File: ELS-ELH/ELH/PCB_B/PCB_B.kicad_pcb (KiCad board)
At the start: 2 copper layers, 95 x 95 mm, 47 parts, among them J10 Conn_01x07_Pin, J11 Conn_01x08_Pin, J13 Conn_01x06_Pin, J14 TX2 3V3, J15 RX2 3V3, J16 TX2 5V, J17 RX2 5V, J18 Conn_01x06_Pin, J2 GPS Connector, J3 Conn_01x20_Pin, J4 Conn_01x20_Pin, J7 I2C Bus Connector 3, J8 I2C Bus Connector 2, J9 I2C Bus Connector 1, U1 GY-87

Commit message: PCB B ready, PCB A layout ready
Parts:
- removed J10: Conn_01x07_Pin, Connector_PinHeader_2.54mm:PinHeader_1x07_P2.54mm_Vertical
- J3, J4: footprint Connector_PinHeader_2.54mm:PinHeader_1x20_P2.54mm_Vertical -> Connector_PinSocket_2.54mm:PinSocket_1x20_P2.54mm_Vertical

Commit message: Finish PCB B
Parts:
- added J10: Conn_01x07_Pin, Connector_PinHeader_2.54mm:PinHeader_1x07_P2.54mm_Vertical, F.Cu at (73.1, -0.53)
- turned R1 to 80 degrees
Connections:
- ESP1 pad D2: /D2_ESP_MAIN_3V3 -> /CS_SD_ESP_MAIN_3V3
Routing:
- net /CS_SD_ESP_MAIN_3V3: track 0.00 -> 73.7 mm, vias 0 -> 2
- net +5V_MCU: track 195.8 -> 194.4 mm
- net Net-(ESP2-PadD34): track 63.4 -> 62.7 mm

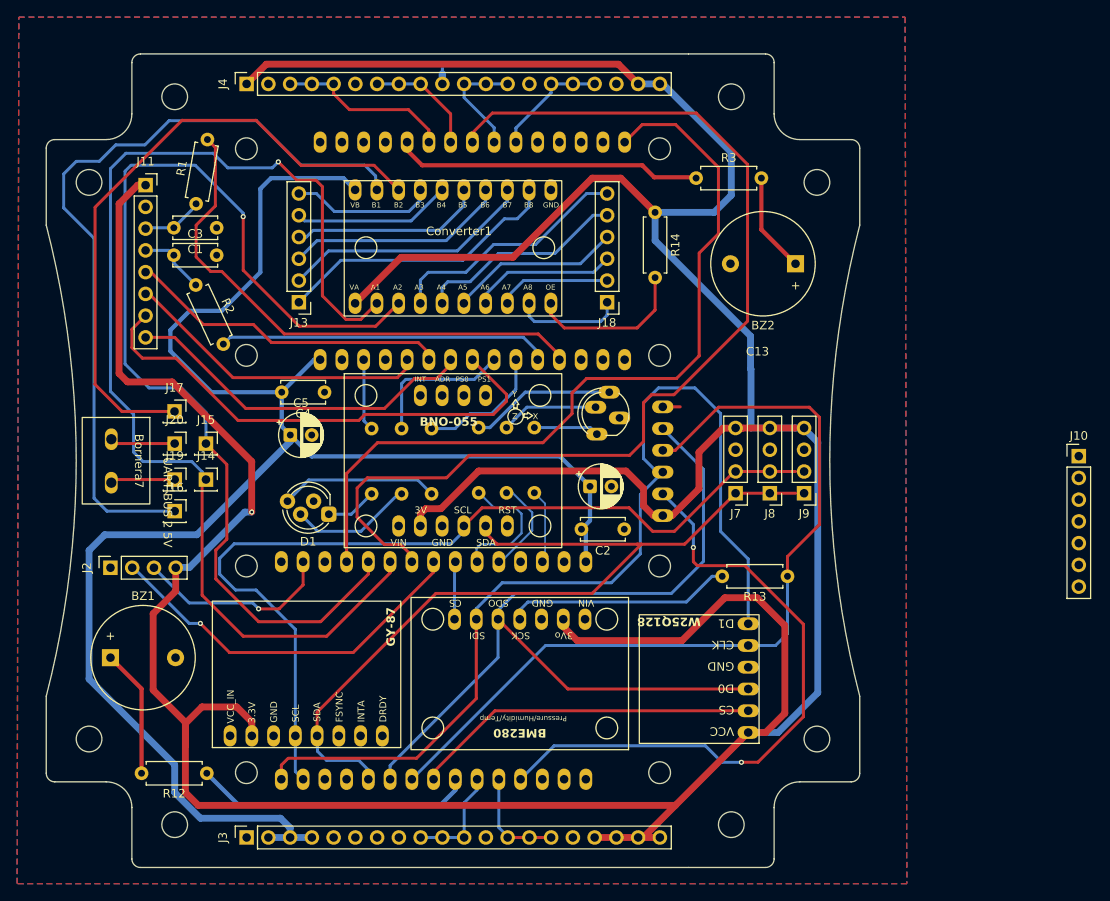
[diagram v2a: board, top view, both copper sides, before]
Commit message: Solve DRC problems with B
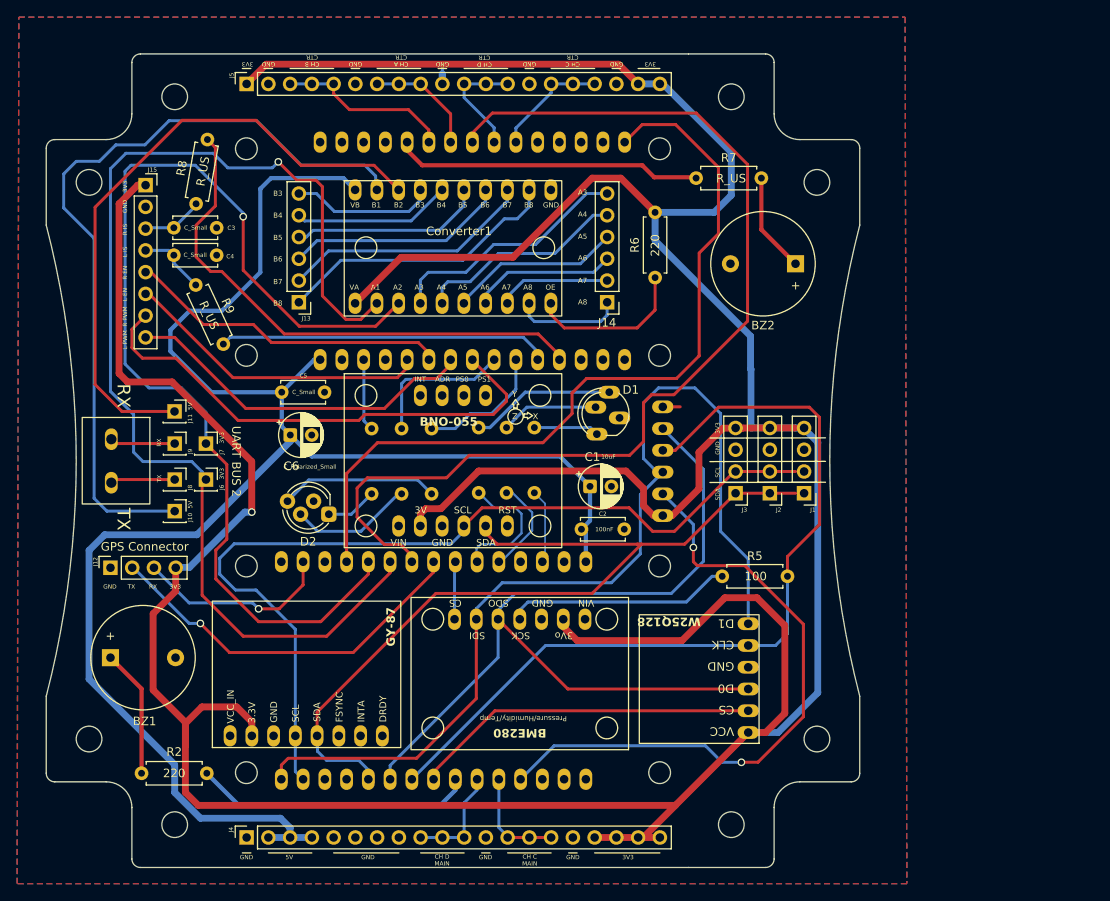
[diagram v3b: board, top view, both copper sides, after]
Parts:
- removed the J10 at (73.1, -0.53)
- Bornera1: renamed from Bornera7; value UART BUS 2 5V -> UART BUS 2
- R10: renamed from R6; value R_US -> 330
- R11: renamed from R8; value R_US -> 330
- R12: renamed from R9; value R_US -> 330
- renumbered BME2 to BME1, C13 to C1, C1 to C3, C3 to C4, C4 to C5, C5 to C6, D10 to D1, D1 to D2, ESP2 to ESP_CTR1, ESP1 to ESP_MAIN1, IMU3 to IMU1, J9 to J1, J16 to J10, J17 to J11, J2 to J12, J18 to J14, J11 to J15, J8 to J2, J7 to J3, J3 to J4, J4 to J5, J14 to J6, J15 to J7, J19 to J8, J20 to J9, R7 to R1, R12 to R2, R5 to R3, R13 to R5, R14 to R6, R3 to R7, R1 to R8, R2 to R9
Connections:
- ESP_MAIN1 pad D12: /D12_ESP_ESP_MAIN_3V3 -> unconnected-(ESP_MAIN1-PadD12)
- ESP_MAIN1 pad D15: /D15_ESP_MAIN_3V3 -> unconnected-(ESP_MAIN1-PadD15)
- ESP_MAIN1 pad EN: /EN_ESP_MAIN_3V3 -> unconnected-(ESP_MAIN1-PadEN)
- ESP_MAIN1 pad RX0: /RX0_ESP_MAIN_3V3 -> unconnected-(ESP_MAIN1-PadRX0)
- ESP_MAIN1 pad TX0: /TX0_ESP_ESP_MAIN_3V3 -> unconnected-(ESP_MAIN1-PadTX0)
- ESP_MAIN1 pad VN: /D39_ESP_ESP_MAIN_3V3 -> unconnected-(ESP_MAIN1-39/VN-PadVN)
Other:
- board text added: "3V3"
- board text added: "5V"
- board text added: "A3"
- board text added: "A4"
- board text added: "A5"
- board text added: "A6"
- board text added: "A7"
- board text added: "A8"
- board text added: "B3"
- board text added: "B4"
- board text added: "B5"
- board text added: "B6"
- board text added: "B7"
- board text added: "B8"
- board text added: "CH A CTR"
- board text added: "CH B CTR"
- board text added: "CH C CTR"
- board text added: "CH C MAIN"
- board text added: "CH D CTR"
- board text added: "CH D MAIN"
- board text added: "GND"
- board text added: "L EN"
- board text added: "L IS"
- board text added: "L PWM"
- board text added: "R EN"
- board text added: "R IS"
- board text added: "R PWM"
- board text added: "RX"
- board text added: "SCL"
- board text added: "SDA"
- board text added: "TX"

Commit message: Update almost finished
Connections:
- ESP_CTR1 pad D19: /CH_C_MOSFET_ESP_CTR_3V3 -> /CH_A_MOSFET_ESP_CTR_3V3
- ESP_CTR1 pad TX2: /CH_A_MOSFET_ESP_CTR_3V3 -> /CH_C_MOSFET_ESP_CTR_3V3
- J5 pad 15: /CH_C_MOSFET_ESP_CTR_3V3 -> /CH_A_MOSFET_ESP_CTR_3V3
- J5 pad 16: /CH_C_MOSFET_ESP_CTR_3V3 -> /CH_A_MOSFET_ESP_CTR_3V3
- J5 pad 17: /CH_C_MOSFET_ESP_CTR_3V3 -> /CH_A_MOSFET_ESP_CTR_3V3
- J5 pad 7: /CH_A_MOSFET_ESP_CTR_3V3 -> /CH_C_MOSFET_ESP_CTR_3V3
- J5 pad 8: /CH_A_MOSFET_ESP_CTR_3V3 -> /CH_C_MOSFET_ESP_CTR_3V3
- J5 pad 9: /CH_A_MOSFET_ESP_CTR_3V3 -> /CH_C_MOSFET_ESP_CTR_3V3

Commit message: Finished the manufacture
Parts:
- removed J10: TX2 5V, Connector_PinSocket_2.54mm:PinSocket_1x01_P2.54mm_Vertical
- removed J11: RX2 5V, Connector_PinSocket_2.54mm:PinSocket_1x01_P2.54mm_Vertical
- removed J7: RX2 3V3, Connector_PinSocket_2.54mm:PinSocket_1x01_P2.54mm_Vertical
- removed J8, J9: ~, Connector_PinSocket_2.54mm:PinSocket_1x01_P2.54mm_Vertical
- added G***: LOGO, ELH_Library:deltav_logo, B.Cu at (32.9, -18.5)
- added G***: LOGO, ELH_Library:IREC, B.Cu at (35.8, -13.0)
- added G***: LOGO, ELH_Library:volta_logo, B.Cu at (38.4, -18.6)
- added J16: Conn_02x04_Odd_Even, Connector_PinHeader_2.54mm:PinHeader_2x04_P2.54mm_Vertical, F.Cu at (-33.2, -3.78)
- C3, C4: value C_Small -> ???
- C5: value C_Small -> 100nF
- C6: value C_Polarized_Small -> 10uF
- J6: value TX2 3V3 -> Conn_01x02_Pin; footprint Connector_PinSocket_2.54mm:PinSocket_1x01_P2.54mm_Vertical -> Connector_PinHeader_2.54mm:PinHeader_1x02_P2.54mm_Vertical
- R7: value R_US -> 220
- R8, R9: value R_US -> ???
- moved J6 68.7 mm to (31.2, 35.5)
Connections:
- ESP_MAIN1 pad 3V3: unconnected-(ESP_MAIN1-Pad3V3) -> +3.3V_ESP_MAIN
- J6 pad 1: /TX_UART_BUS2_ESP_MAIN_3V3 -> +3.3V_ESP_MAIN
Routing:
- net +3.3V_ESP_MAIN: track 0.00 -> 18.2 mm
- net /SCL_I2C_BUS1_ESP_MAIN_3V3: track 105.3 -> 113.9 mm
- net /RX_UART_BUS2_ESP_MAIN_3V3: track 123.9 -> 126.6 mm
- net /CS_SD_ESP_MAIN_3V3: track 73.7 -> 72.1 mm
- net /SDA_I2C_BUS1_ESP_MAIN_3V3: track 99.1 -> 100.1 mm
- net +3.3V_SENSORS: track 487.2 -> 488.1 mm
- net +5V_MCU: track 194.4 -> 193.6 mm
- net GND: track 3.88 -> 3.21 mm
- net /TX_UART_BUS2_ESP_MAIN_3V3: track 134.3 -> 133.8 mm
- net Net-(Bornera1-Pin_2): track 7.55 -> 7.03 mm
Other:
- board text added: "X"
